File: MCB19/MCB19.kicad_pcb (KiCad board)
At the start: 2 copper layers, 94 parts, among them J401 USART, J402 DISABLE, J601 RJ45, J602 RJ45, J611 +BATT, J612 GND, J613 VBAT+, J614 VBAT-, Q601 IRFP260N, Q602 IRFP260N, U201 MCP2551-I/SN, U202 MCP2515-xSO, U301 LM7805, U401 ATMEGA328P-PU, U501 LM7815, U601 LM5104MNOPB, U602 INA211_DCK_6, U603 LM324, Y201 16MHz, Y401 16MHz

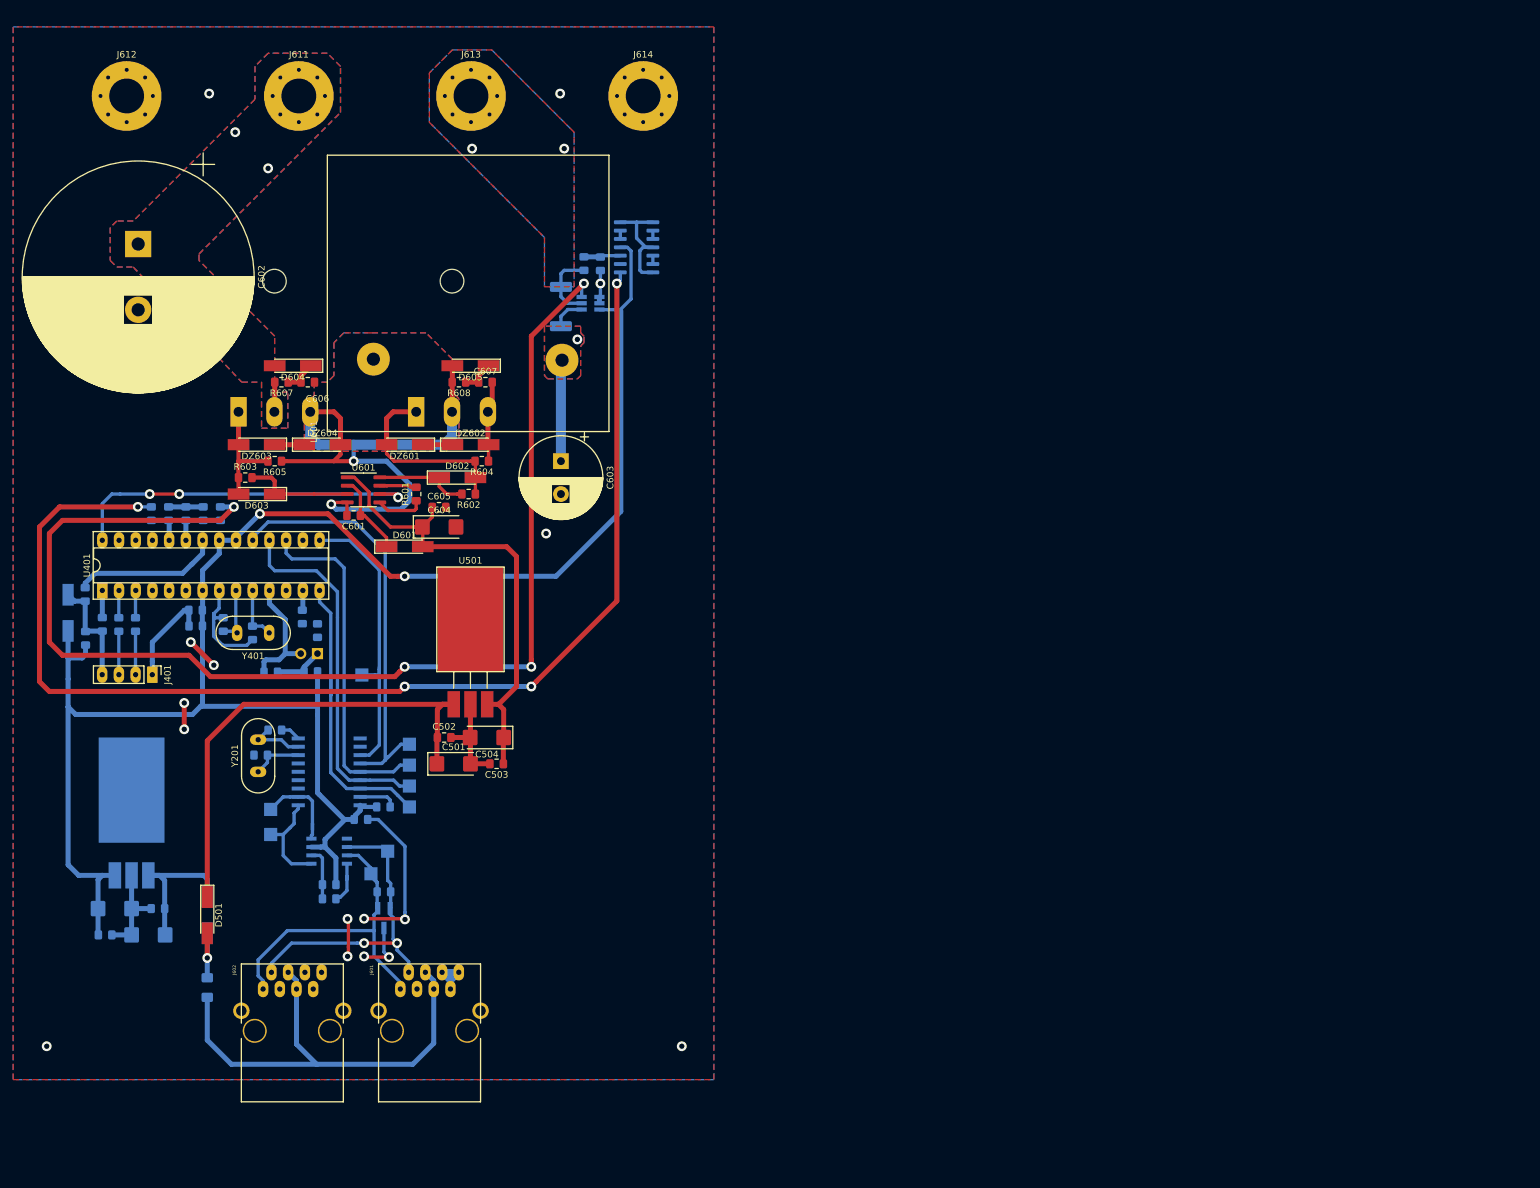
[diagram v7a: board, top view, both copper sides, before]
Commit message: Esquemático corrigido, layout retrabalhado.
No esquemático foram adicionados alguns capacitores para os opamps e aumentado a quantidade de capacitores na saída. Alguns detalhes de regras elétricas relacionadas aos PWR_FLAGs foram corrigidos.
Para o layout, na tentativa de encontrar um roteamento mais simples e claro, no qual fosse possível desenhar o caminho das correntes das malhas, utilizando o PMP7165 da Texas Instruments como referência.
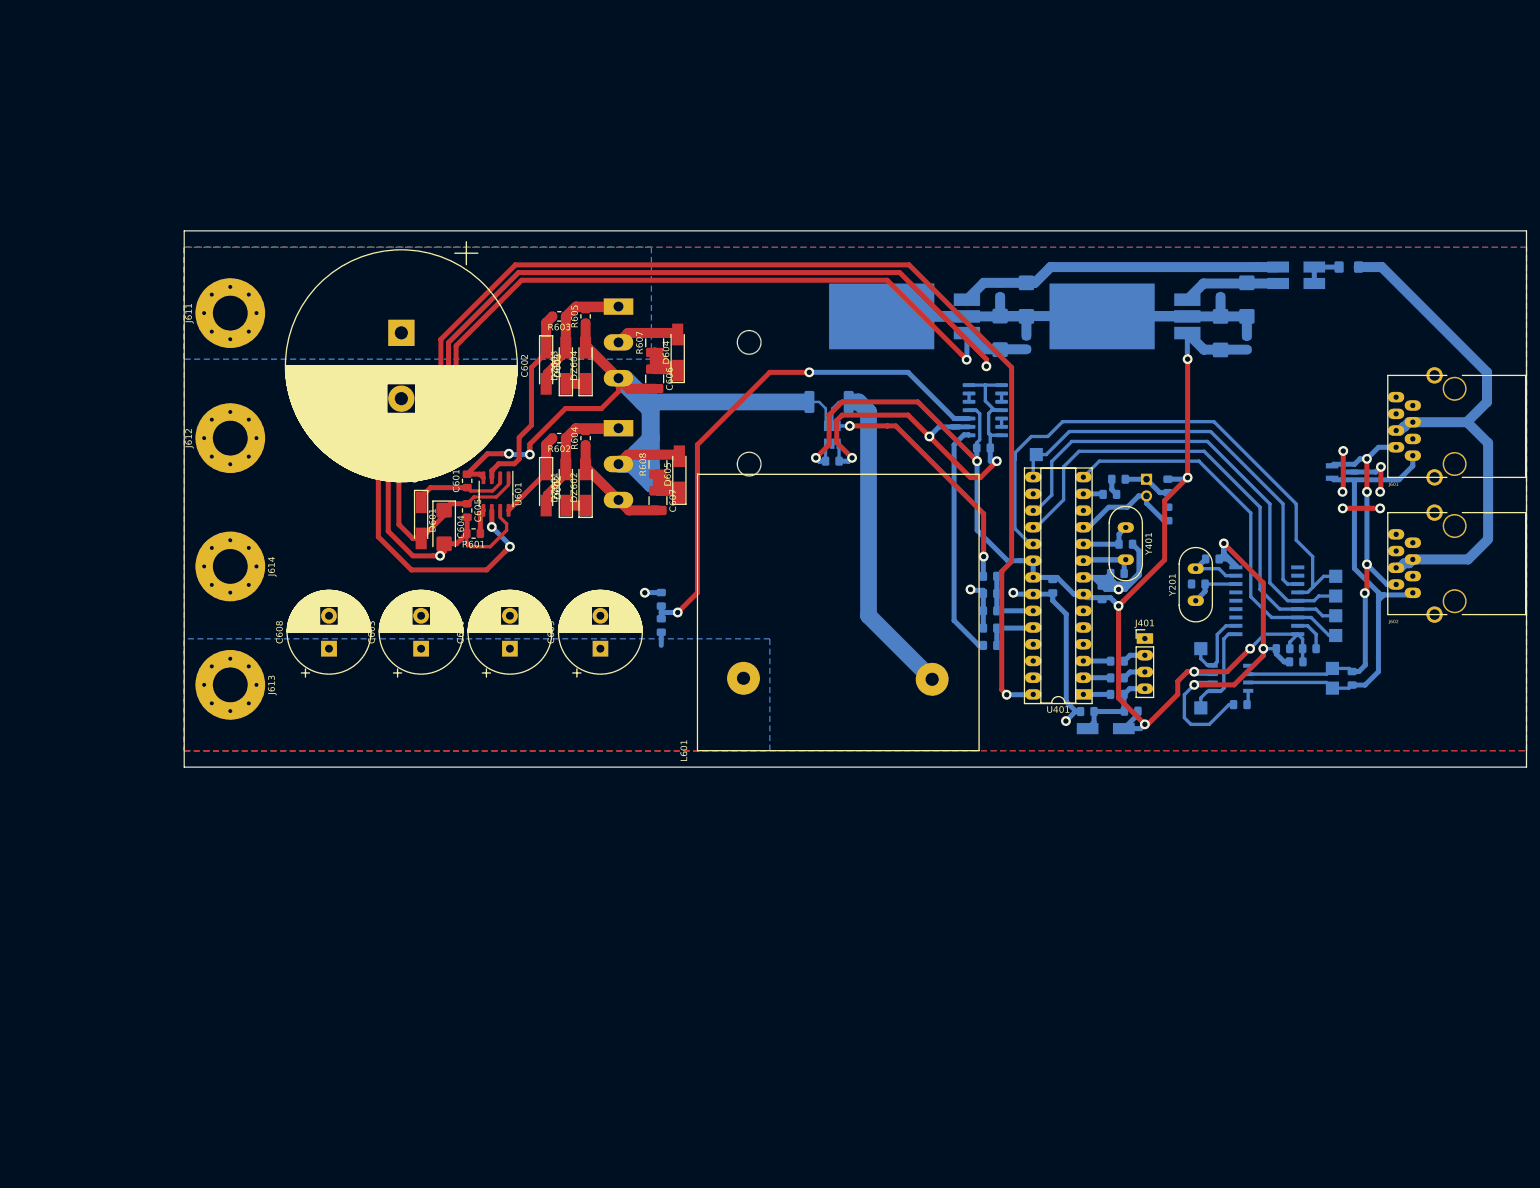
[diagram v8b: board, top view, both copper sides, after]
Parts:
- added C608: 47uF, Capacitor_THT:CP_Radial_D12.5mm_P5.00mm, F.Cu at (72.0, 114.0)
- added C609: 47uF, Capacitor_THT:CP_Radial_D12.5mm_P5.00mm, F.Cu at (113.2, 114.0)
- added C610: 47uF, Capacitor_THT:CP_Radial_D12.5mm_P5.00mm, F.Cu at (99.5, 114.0)
- added C611: 100nF, Capacitor_SMD:C_0805_2012Metric_Pad1.15x1.40mm_HandSolder, B.Cu at (148.5, 85.5)
- added C612: 100nF, Capacitor_SMD:C_0805_2012Metric_Pad1.15x1.40mm_HandSolder, B.Cu at (171.5, 83.5)
- C501, C502, C503, C504, D501, U501: moved to B.Cu
- C606, C607: footprint Capacitor_SMD:C_0805_2012Metric_Pad1.15x1.40mm_HandSolder -> Capacitor_SMD:C_1210_3225Metric_Pad1.42x2.65mm_HandSolder
- J611: value +BATT -> +BAT_IN
- J612: value GND -> -BAT_IN
- J613: value VBAT+ -> +BAT_OUT
- J614: value VBAT- -> -BAT_OUT
- R607, R608: footprint Resistor_SMD:R_0805_2012Metric_Pad1.15x1.40mm_HandSolder -> Resistor_SMD:R_1210_3225Metric_Pad1.42x2.65mm_HandSolder
- moved F501 205.2 mm to (227.0, 56.0), turned to 0 degrees
- moved C303 195.5 mm to (211.5, 67.5), turned to 90 degrees
- moved C301 192.9 mm to (211.5, 61.0), turned to 270 degrees
- moved D501 192.6 mm to (219.0, 56.0), turned to 0 degrees
- moved D301 191.3 mm to (219.0, 58.5), turned to 0 degrees
- moved C304 189.4 mm to (207.5, 66.0), turned to 90 degrees
- moved C302 186.9 mm to (207.5, 59.5), turned to 270 degrees
- moved J602 184.8 mm to (236.7, 105.5), turned to 90 degrees
- moved U301 178.8 mm to (201.2, 61.0), turned to 270 degrees
- moved J601 173.9 mm to (236.7, 84.7), turned to 90 degrees
- moved D201 160.6 mm to (225.9, 87.2), turned to 0 degrees
- moved R401 159.3 mm to (193.9, 123.5), turned to 0 degrees
- moved D401 158.7 mm to (190.1, 126.2), turned to 180 degrees
- moved R411 154.6 mm to (191.8, 121.0), turned to 180 degrees
- moved C406 153.3 mm to (187.2, 123.5), turned to 180 degrees
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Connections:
- J613 pad 1: Net-(J613-Pad1) -> Net-(C603-Pad1)
- L601 pad 1: Net-(C601-Pad2) -> Net-(C603-Pad1)
- L601 pad 2: Net-(C603-Pad1) -> Net-(L601-Pad2)
- R606 pad 1: Net-(J613-Pad1) -> Net-(L601-Pad2)
- R606 pad 2: Net-(C603-Pad1) -> Net-(C601-Pad2)
- R610 pad 1: Net-(J613-Pad1) -> Net-(C603-Pad1)
- U201 pad 5: Net-(U201-Pad5) -> (no net)
- U202 pad 10: Net-(U202-Pad10) -> (no net)
- U202 pad 11: Net-(U202-Pad11) -> (no net)
- U202 pad 3: Net-(U202-Pad3) -> (no net)
- U202 pad 4: Net-(U202-Pad4) -> (no net)
- U202 pad 5: Net-(U202-Pad5) -> (no net)
- U202 pad 6: Net-(U202-Pad6) -> (no net)
- U401 pad 12: Net-(U401-Pad12) -> (no net)
- U401 pad 16: Net-(U401-Pad16) -> (no net)
- U401 pad 25: Net-(U401-Pad25) -> (no net)
- U401 pad 26: Net-(U401-Pad26) -> (no net)
- U401 pad 27: Net-(U401-Pad27) -> (no net)
- U401 pad 4: Net-(U401-Pad4) -> (no net)
- U401 pad 5: Net-(U401-Pad5) -> (no net)
- U401 pad 6: Net-(U401-Pad6) -> (no net)
- U602 pad 4: Net-(C603-Pad1) -> Net-(C601-Pad2)
- U602 pad 5: Net-(J613-Pad1) -> Net-(L601-Pad2)
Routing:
- net GND: track 205.2 -> 545.9 mm, vias 16 -> 20
- net /MCU/PWM: track 54.6 -> 217.1 mm
- net /driver/LM324A: track 186.0 -> 35.7 mm, vias 4 -> 0
- net /MCU/INALLL: track 188.1 -> 38.8 mm, vias 4 -> 2
- net +15V: track 72.0 -> 158.1 mm, vias 0 -> 1
- net Net-(R609-Pad2): track 5.62 -> 82.2 mm, vias 0 -> 2
- net +5V: track 283.3 -> 212.2 mm, vias 2 -> 8
- net Net-(L601-Pad2): track 0.00 -> 53.3 mm
- net Net-(C601-Pad2): track 93.3 -> 145.5 mm
- net /CANBUS CONN/CAN_H: track 50.6 -> 78.6 mm
- net Net-(C501-Pad1): track 74.6 -> 49.4 mm
- net /CANBUS CONN/CAN_18V: track 70.9 -> 93.8 mm
- net /SCK: track 63.8 -> 86.3 mm
- net /CANBUS CONN/CAN_L: track 48.2 -> 67.1 mm, vias 2 -> 4
- net Net-(C603-Pad1): track 20.7 -> 2.00 mm, vias 1 -> 0
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- removed copper zone on F.Cu, net +BATT
- removed copper zone on B.Cu, net Net-(C601-Pad2)
- removed copper zone on F.Cu, net Net-(C601-Pad2)
- removed copper zone on F.Cu, net Net-(C603-Pad1)
- removed copper zone on B.Cu, net Net-(J613-Pad1)
- removed copper zone on F.Cu, net Net-(J613-Pad1)
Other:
- board outline added: 204 x 81.5 mm
